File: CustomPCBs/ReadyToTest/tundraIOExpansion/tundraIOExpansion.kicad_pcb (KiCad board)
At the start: 4 copper layers, 46 x 36.5 mm, 58 parts, among them J1 Conn_01x25, J2 Conn_ARM_SWD_TagConnect_TC203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, J3 Conn_ARM_SWD_TagConnect_TC203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, U1 RP2040, U2 MX25L3233FM2, U4 MX25L3233FM2, U5 RP2040, Y1 12.000MHz, Y2 12.000MHz, Y3 32.768kHz

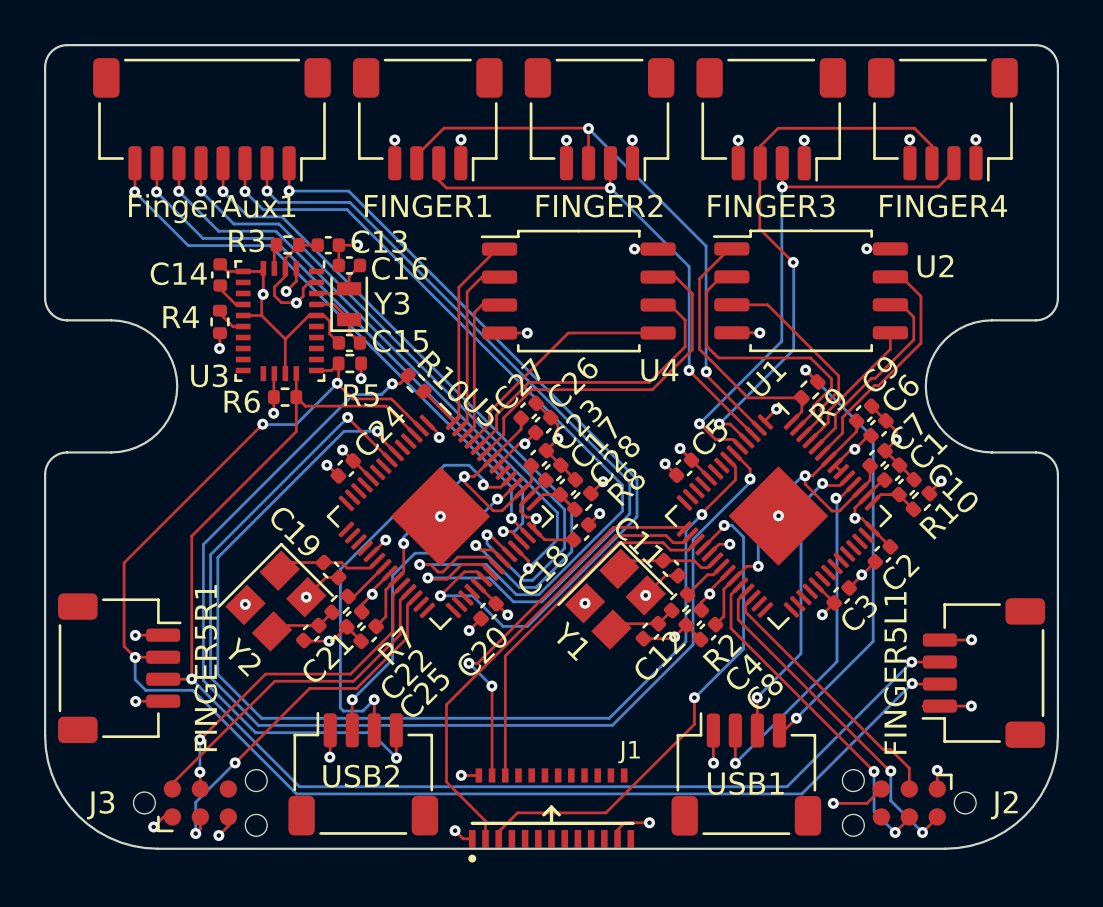
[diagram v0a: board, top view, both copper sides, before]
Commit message: Fixing mistakes on the main board
Flash chip was not the recommended by raspberry pi foundation - fixed.
SCL and SDA pins on the thumb JST connectors were switched - fixed.
MOSI and MISO pins on the RP2040 were switched - fixed.
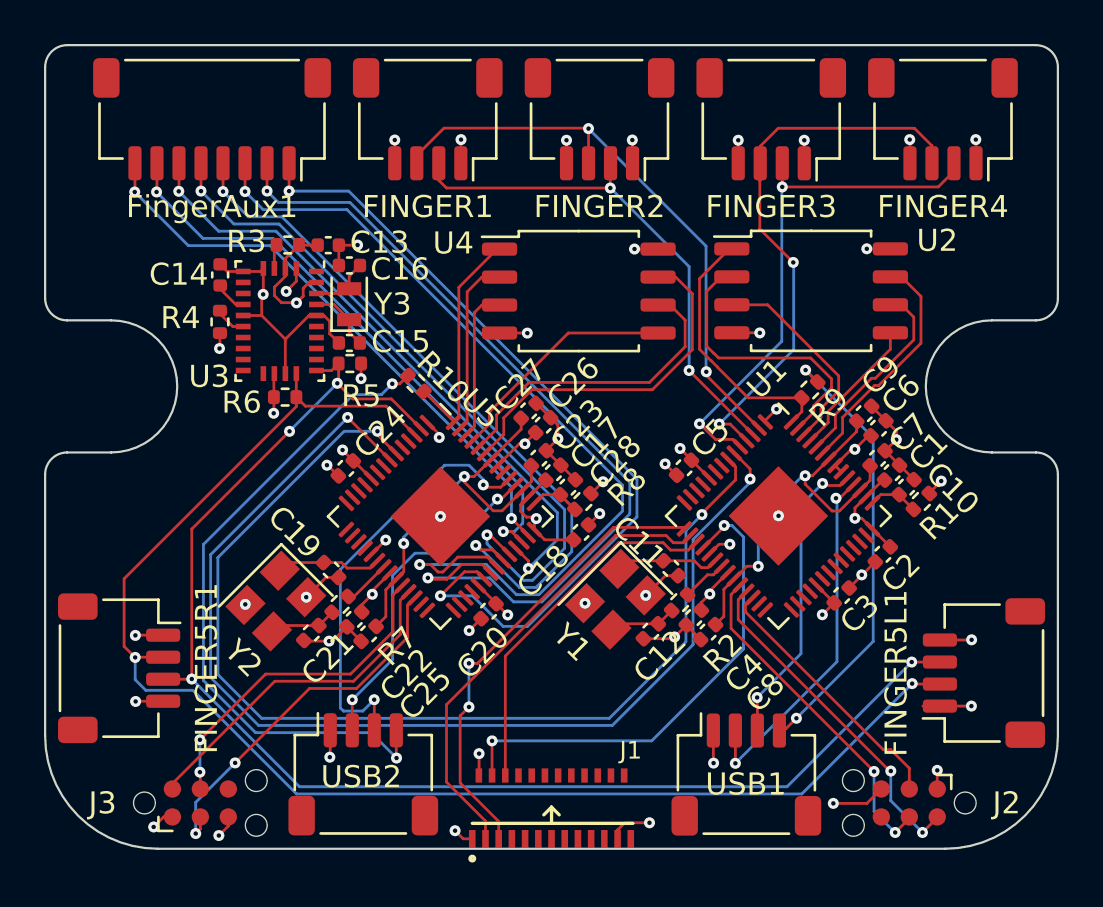
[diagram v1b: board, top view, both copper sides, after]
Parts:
- U2, U4: value MX25L3233FM2 -> W25Q32JVSS; footprint Package_SO:SOP-8_5.28x5.23mm_P1.27mm -> Package_SO:SOIC-8_5.23x5.23mm_P1.27mm
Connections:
- R5 pad 2: Net-(FINGER5L1-Pin_2) -> Net-(FINGER5L1-Pin_3)
- R6 pad 2: Net-(FINGER5L1-Pin_3) -> Net-(FINGER5L1-Pin_2)
- U1 pad 15: D12-MI_MISO -> D11-MI_MOSI
- U1 pad 18: D11-MI_MOSI -> D12-MI_MISO
- U3 pad 19: Net-(FINGER5L1-Pin_3) -> Net-(FINGER5L1-Pin_2)
- U3 pad 20: Net-(FINGER5L1-Pin_2) -> Net-(FINGER5L1-Pin_3)
- U5 pad 2: Net-(FINGER5L1-Pin_2) -> Net-(FINGER5L1-Pin_3)
- U5 pad 3: Net-(FINGER5L1-Pin_3) -> Net-(FINGER5L1-Pin_2)
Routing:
- net D12-MI_MISO: track 17.9 -> 22.3 mm
- net D11-MI_MOSI: track 23.2 -> 21.2 mm
- net Net-(FINGER5L1-Pin_2): track 67.4 -> 65.5 mm, vias 4 -> 2
- net Net-(FINGER5L1-Pin_3): track 61.6 -> 62.6 mm, vias 2 -> 4

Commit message: Fixing USB connectors on main board
Forgot to invert the USB connectors, these were wrong too on the first
batch.
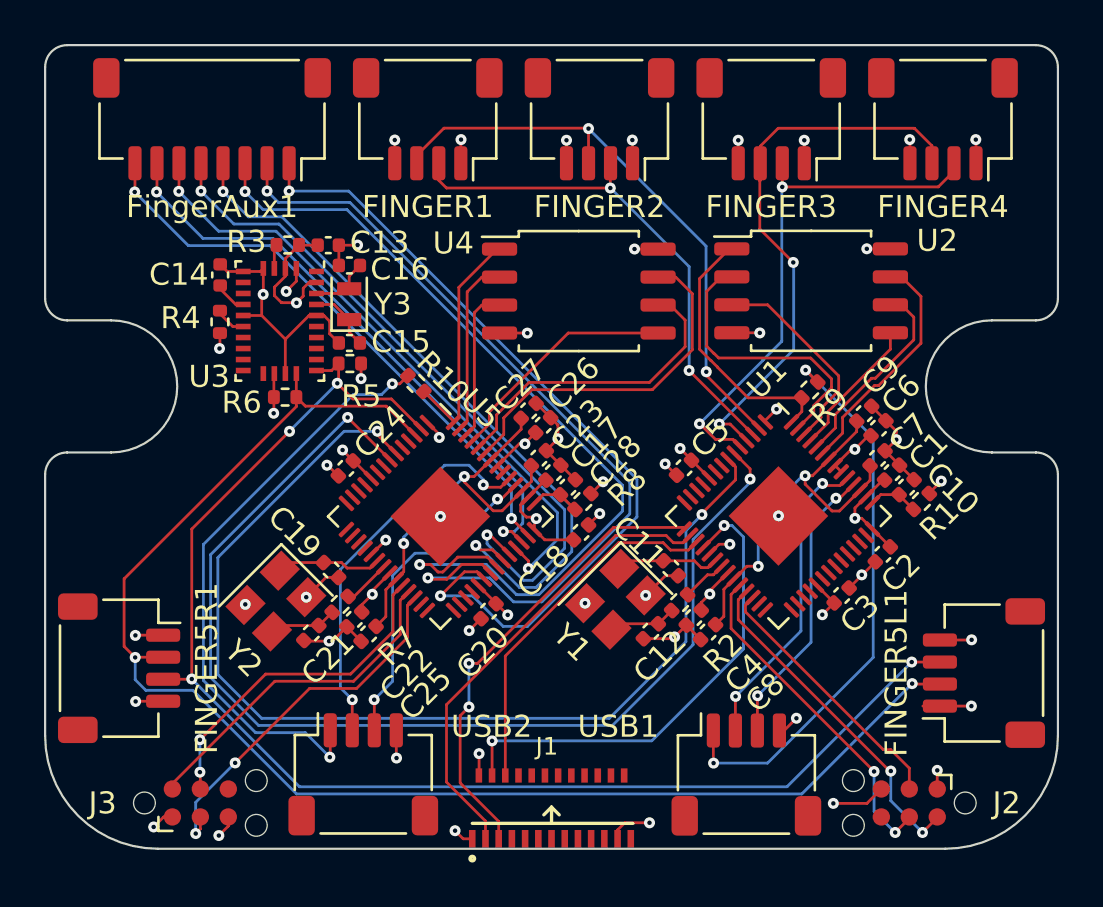
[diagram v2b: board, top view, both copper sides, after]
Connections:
- R10 pad 2: Net-(USB2-Pin_4) -> Net-(USB2-Pin_1)
- R9 pad 2: Net-(USB1-Pin_4) -> Net-(USB1-Pin_1)
- USB1 pad 1: GND -> Net-(USB1-Pin_1)
- USB1 pad 2: Net-(U1-USB_DM) -> Net-(U1-USB_DP)
- USB1 pad 3: Net-(U1-USB_DP) -> Net-(U1-USB_DM)
- USB1 pad 4: Net-(USB1-Pin_4) -> GND
- USB2 pad 1: GND -> Net-(USB2-Pin_1)
- USB2 pad 2: Net-(U5-USB_DM) -> Net-(U5-USB_DP)
- USB2 pad 3: Net-(U5-USB_DP) -> Net-(U5-USB_DM)
- USB2 pad 4: Net-(USB2-Pin_4) -> GND
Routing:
- net Net-(USB2-Pin_4): track 30.1 -> 0.00 mm, vias 2 -> 0
- net Net-(USB2-Pin_1): track 0.00 -> 27.1 mm, vias 0 -> 2
- net Net-(USB1-Pin_1): track 0.00 -> 25.8 mm, vias 0 -> 2
- net Net-(USB1-Pin_4): track 20.3 -> 0.00 mm, vias 2 -> 0
- net Net-(U1-USB_DM): track 16.5 -> 13.2 mm
- net Net-(U5-USB_DP): track 19.9 -> 17.9 mm
